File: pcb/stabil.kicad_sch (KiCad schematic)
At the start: 51 parts, among them Q10 IRFR5305, U11 TPS5430DDA, U12 LM75B, U13 INA219AxD, U16 TSV911IDT, U17 PC817, U18 LM75B, U19 TPS5430DDA

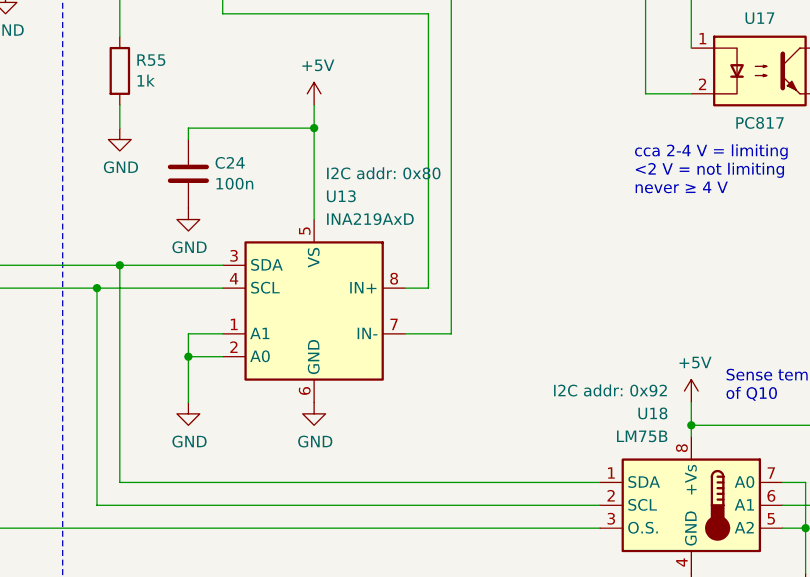
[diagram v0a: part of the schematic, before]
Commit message: Use ATmega328pb instead of ATmega328p.
Reason: obtain some free pins as a reserve.
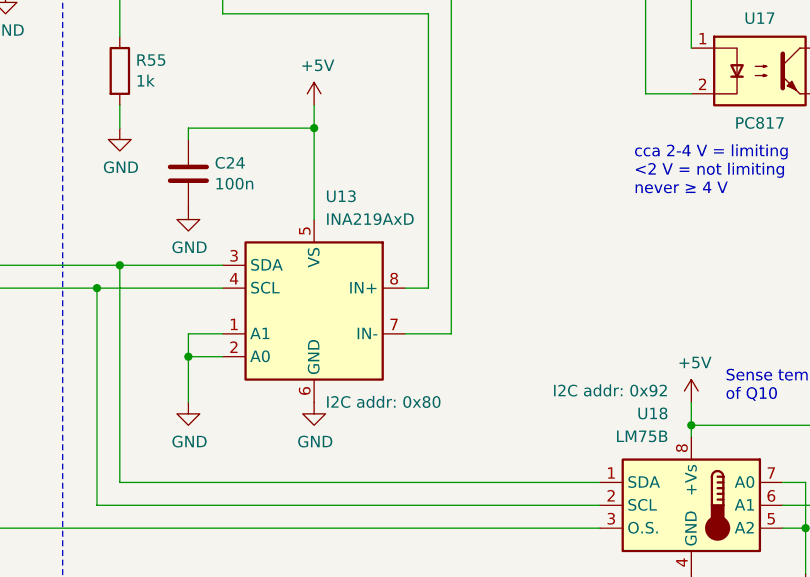
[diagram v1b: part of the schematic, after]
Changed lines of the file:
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@@
 		)
 		(property "I2C addr" "0x80"
-			(at 207.01 92.71 0)
+			(at 207.01 118.11 0)
 			(show_name yes)
 			(effects
